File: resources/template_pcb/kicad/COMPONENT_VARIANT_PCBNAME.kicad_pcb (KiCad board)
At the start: 2 copper layers, 65 x 56 mm, 5 parts, among them P1 Conn_02x20_Odd_Even

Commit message: update check lists
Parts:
- added MK5: M2.5, MountingHole:MountingHole_2.7mm_M2.5, F.Cu at (203.5, 146.5)
- added MK6: M2.5, MountingHole:MountingHole_2.7mm_M2.5, F.Cu at (261.5, 146.5)
- moved MK3 26.0 mm to (203.5, 120.5)
- moved MK4 26.0 mm to (261.5, 120.5)
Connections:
- net /GPIO10(SPI0_MOSI) renamed /SENS_MOSI
- net /GPIO11(SPI0_SCK) renamed /SENS_SCLK
- net /GPIO14(TXD0) renamed /SENS_GPIO0
- net /GPIO15(RXD0) renamed /SENS_GPIO1
- net /GPIO17(GEN0) renamed /SENS_INT_ECG
- net /GPIO18(GEN1)(PWM0) renamed /SENS_INT_SPO2
- net /GPIO2(SDA1) renamed /SENS_SDA
- net /GPIO22(GEN3) renamed /~SENS_RST_BPM
- net /GPIO23(GEN4) renamed /~SENS_RST_ECG
- net /GPIO24(GEN5) renamed /~SENS_RST_SPO2
- net /GPIO25(GEN6) renamed /~SENS_CS_BPM
- net /GPIO27(GEN2) renamed /SENS_START
- net /GPIO3(SCL1) renamed /SENS_SCL
- net /GPIO4(GCLK) renamed /SENS_INT_BPM
- net /GPIO7(SPI1_CE_N) renamed /~SENS_CS_SPO2
- net /GPIO8(SPI0_CE_N) renamed /~SENS_CS_ECG
- net /GPIO9(SPI0_MISO) renamed /SENS_MISO
- P1 pad 1: +3V3 -> +3.3VA
- P1 pad 2: +5V -> +5VA
- P1 pad 4: +5V -> +5VD
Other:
- outline, holes or cut-outs redrawn
- board text added: "All connectors except the 40 pin header must be angled and must be placed on this edge pointing downwards."
- board text added: "RASPBERRY-PI 40-PIN ADDON BOARD VIEW FROM TOP NOTE: P1 SHOULD BE FITTED ON THE REVERSE OF THE BOARD NOTE: remove pcb edge below MK3/MK4 or MK5/MK6 depending on the board size you need."
- board text removed: "RASPBERRY-PI 40-PIN ADDON BOARD VIEW FROM TOP NOTE: P1 SHOULD BE FITTED ON THE REVERSE OF THE BOARD ADD EDGE CUTS FROM CAMERA AND DISPLAY PORTS AS REQUIRED"
- board text removed: "RJ45"
- board text removed: "USB"

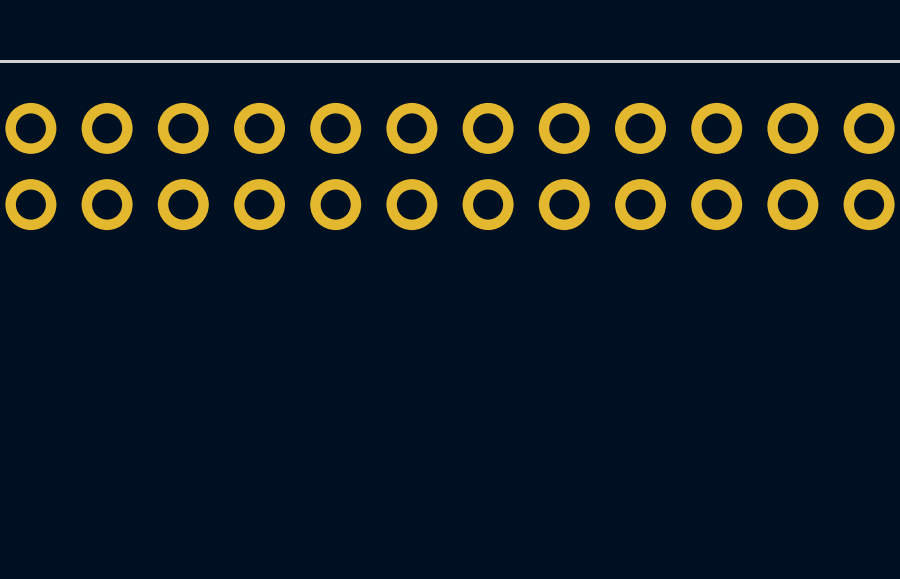
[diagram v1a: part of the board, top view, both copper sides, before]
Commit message: add chip select mux in pcb template
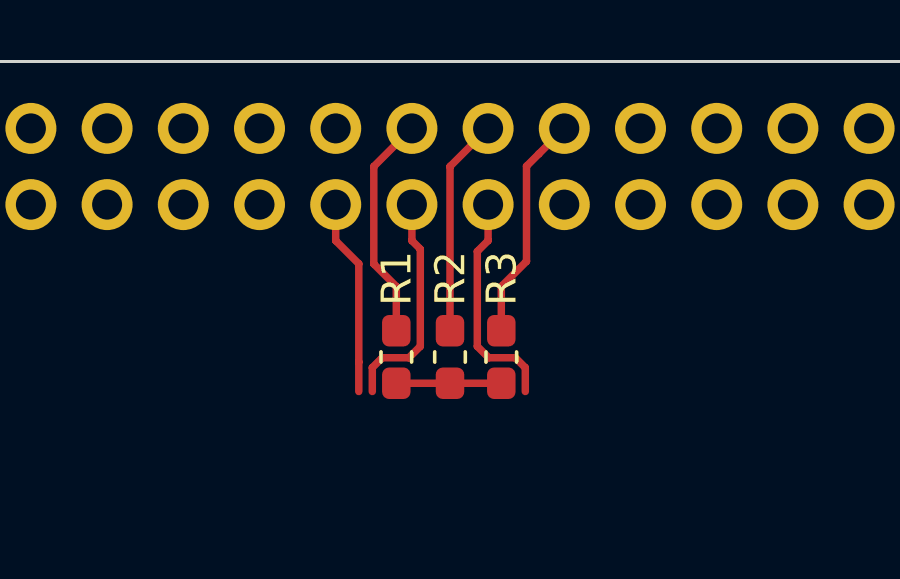
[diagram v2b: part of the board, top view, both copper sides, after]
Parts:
- added R1: n.p., Resistor_SMD:R_0603_1608Metric_Pad1.05x0.95mm_HandSolder, F.Cu at (233.2, 103.8)
- added R2: n.p., Resistor_SMD:R_0603_1608Metric_Pad1.05x0.95mm_HandSolder, F.Cu at (235.0, 103.8)
- added R3: n.p., Resistor_SMD:R_0603_1608Metric_Pad1.05x0.95mm_HandSolder, F.Cu at (236.8, 103.8)
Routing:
- net /~SENS_CS_SPO2: track 0.00 -> 7.61 mm
- net /~SENS_CS_BPM: track 0.00 -> 7.58 mm
- net /SENS_SCLK: track 0.00 -> 7.56 mm
- net /SENS_MISO: track 0.00 -> 7.53 mm
- net /~SENS_CS_ECG: track 0.00 -> 7.27 mm
- net /SENS_MOSI: track 0.00 -> 6.55 mm
- net /~CS: track 0.00 -> 4.05 mm
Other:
- net class Default: via_drill 0.6 -> 0.5
